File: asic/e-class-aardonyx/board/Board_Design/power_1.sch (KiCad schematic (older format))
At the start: 29 parts, among them J5 PJ-202H PWRJACK, J6 Conn_1x3_M, SW1 SW_SPST, U4 TPS54627DDAR

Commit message: updated footprint & tracks
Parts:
- J5: footprint Aardonyx:Pwr_Jack_DC_PJ-202AH_Horizontal -> Aardonyx:CUI_PJ-202AH
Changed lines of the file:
@@
 F 0 "J5" H 3457 2017 50  0000 C CNN
 F 1 "PJ-202H PWRJACK" H 3450 1500 50  0000 C CNN
-F 2 "Aardonyx:Pwr_Jack_DC_PJ-202AH_Horizontal" H 3450 1660 50  0001 C CNN
+F 2 "Aardonyx:CUI_PJ-202AH" H 3450 1660 50  0001 C CNN
 F 3 "https://www.digikey.com/products/en?keywords=PJ-202AH" H 3450 1660 50  0001 C CNN
 F 4 "CONN PWR JACK 2X5.5MM KINKED PIN" H 3400 1700 50  0001 C CNN "Description"

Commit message: updated footprint c37 & f1
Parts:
- C37: footprint Aardonyx:CP_EIA-7260-38_VISHAY_Pad2.68x7.50mm_HandSolder -> Aardonyx:CP_EIA-2924_tcn4227_Pad6.1x7.3mm
- F1: footprint Aardonyx:vishay_ptccl_d1mm_w5mm -> Aardonyx:vishay_ptccl_d12.5mm_w4mm
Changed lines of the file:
@@
 F 0 "C37" H 5100 1950 50  0000 L CNN
 F 1 "220UF,2924" V 5050 1350 50  0000 L CNN
-F 2 "Aardonyx:CP_EIA-7260-38_VISHAY_Pad2.68x7.50mm_HandSolder" H 5100 1850 50  0001 C CNN
+F 2 "Aardonyx:CP_EIA-2924_tcn4227_Pad6.1x7.3mm" H 5100 1850 50  0001 C CNN
 F 3 "https://www.digikey.com/product-detail/en/avx-corporation/TCN4227M025R0100/478-12518-1-ND/9836495" H 5100 1850 50  0001 C CNN
 F 4 "CAP TANT POLY 220UF 25V 2924" H 5100 1850 50  0001 C CNN "Description"
@@
 F 0 "F1" V 4475 1600 50  0000 C CNN
 F 1 "PTCCL13H921DBE" V 4550 1700 50  0000 C CNN
-F 2 "Aardonyx:vishay_ptccl_d1mm_w5mm" H 4750 1400 50  0001 L CNN
+F 2 "Aardonyx:vishay_ptccl_d12.5mm_w4mm" H 4750 1400 50  0001 L CNN
 F 3 "https://www.digikey.in/products/en?keywords=PTCCL13H921DBE" H 4700 1600 50  0001 C CNN
 F 4 "PTC RESET FUSE 30V 920MA RADIAL" H 4700 1600 50  0001 C CNN "Description"

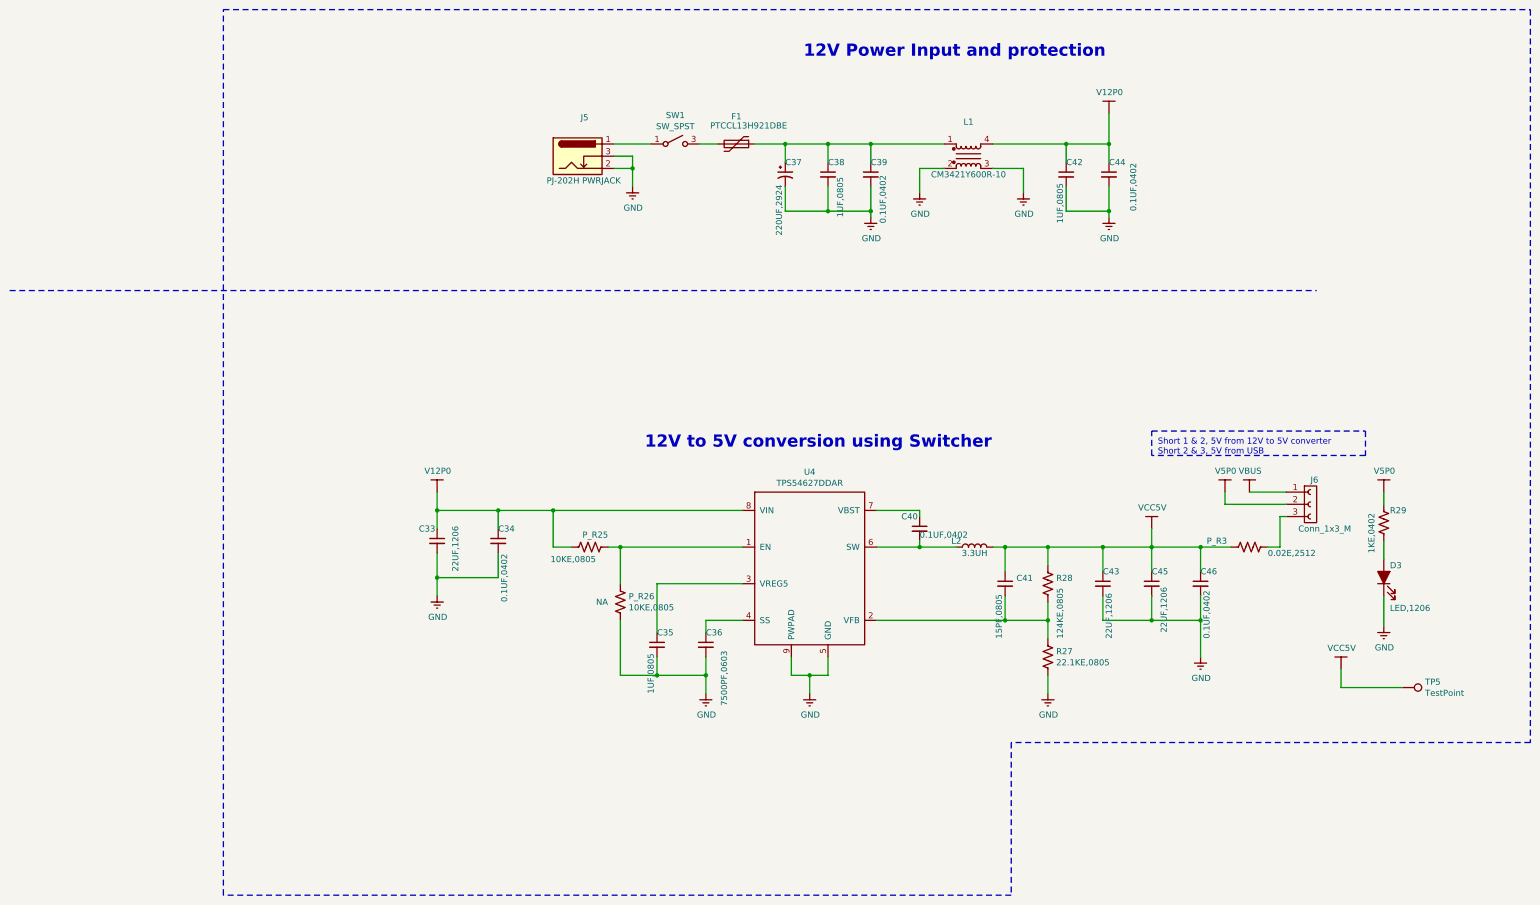
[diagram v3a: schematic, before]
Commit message: Updating layout after back annotation
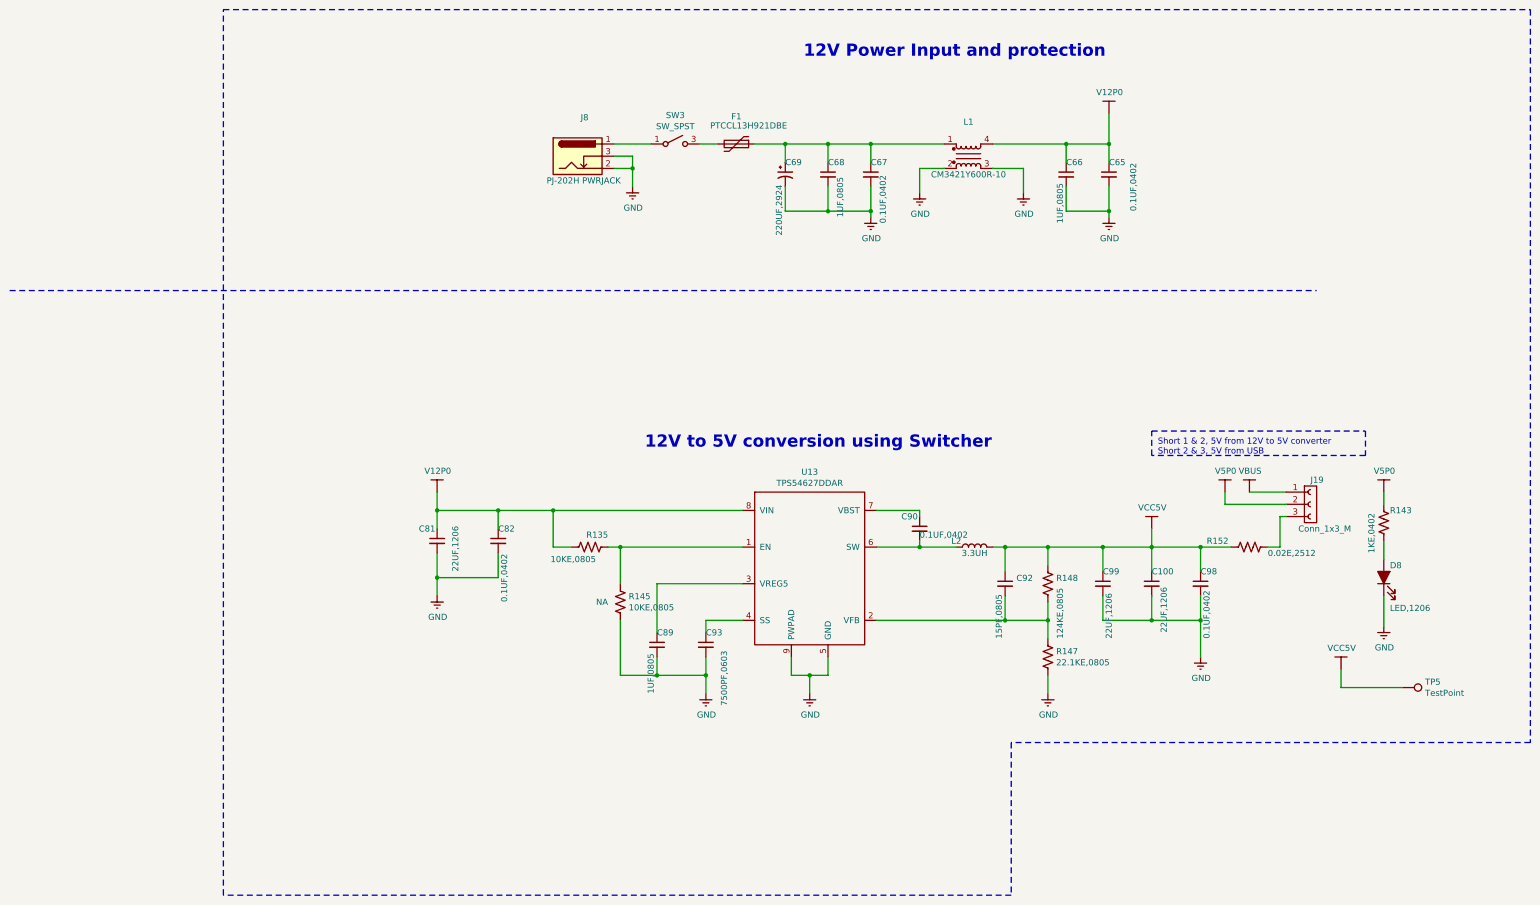
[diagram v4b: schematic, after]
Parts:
- renumbered C45 to C100, C44 to C65, C42 to C66, C39 to C67, C38 to C68, C37 to C69, C33 to C81, C34 to C82, C35 to C89, C40 to C90, C41 to C92, C36 to C93, C46 to C98, C43 to C99, D3 to D8, J6 to J19, J5 to J8, P_R25 to R135, R29 to R143, P_R26 to R145, R27 to R147, R28 to R148, P_R3 to R152, SW1 to SW3, U4 to U13
